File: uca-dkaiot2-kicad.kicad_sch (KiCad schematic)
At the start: 0 parts

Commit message: Continue filling schematics
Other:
- added sheet Input_Output (Input_Output.kicad_sch)
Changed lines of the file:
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@@
 	(title_block
 		(title "UCA DKAIoT2")
-		(date "2026-05-06")
+		(date "2026-05-27")
 		(rev "v0.1")
 		(company "//piernov")
@@
 				)
 			)
+		)
+	)
+	(sheet
+		(at 125.73 97.79)
+		(size 43.18 19.05)
+		(exclude_from_sim no)
+		(in_bom yes)
+		(on_board yes)
+		(dnp no)
+		(fields_autoplaced yes)
+		(stroke
+			(width 0.1524)
+			(type solid)
+		)
+		(fill
+			(color 0 0 0 0)
+		)
+		(property "Sheetname" "Input_Output"
+			(at 125.73 97.0784 0)
+			(show_name no)
+			(do_not_autoplace no)
+			(effects
+				(font
+					(size 1.27 1.27)
+				)
+				(justify left bottom)
+			)
+		)
+		(property "Sheetfile" "Input_Output.kicad_sch"
+			(at 125.73 117.4246 0)
+			(show_name no)
+			(do_not_autoplace no)
+			(effects
+				(font
+					(size 1.27 1.27)
+				)
+				(justify left top)
+			)
+		)
+		(instances
+			(project "uca-dkaiot2-kicad"
+				(path "/13b7de53-ecff-4b32-b513-b5b471d022a3"
+					(page "7")
+				)
+			)

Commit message: PCB component placement according to AIoT2
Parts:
- added H1, H2, H3, H4: MountingHole_Pad, MountingHole:MountingHole_3mm_Pad_Via, symbol Mechanical:MountingHole_Pad
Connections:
- new net GND: H1.1, H2.1, H3.1, H4.1

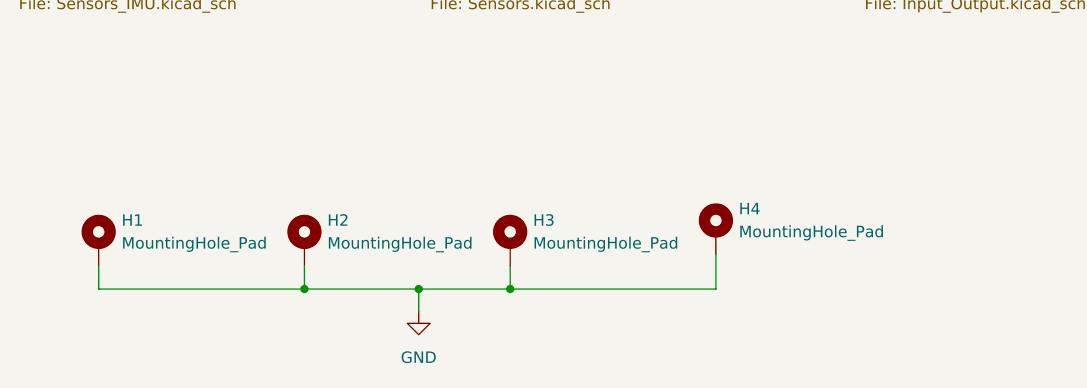
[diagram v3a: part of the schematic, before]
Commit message: pcb: start 2-layer routing
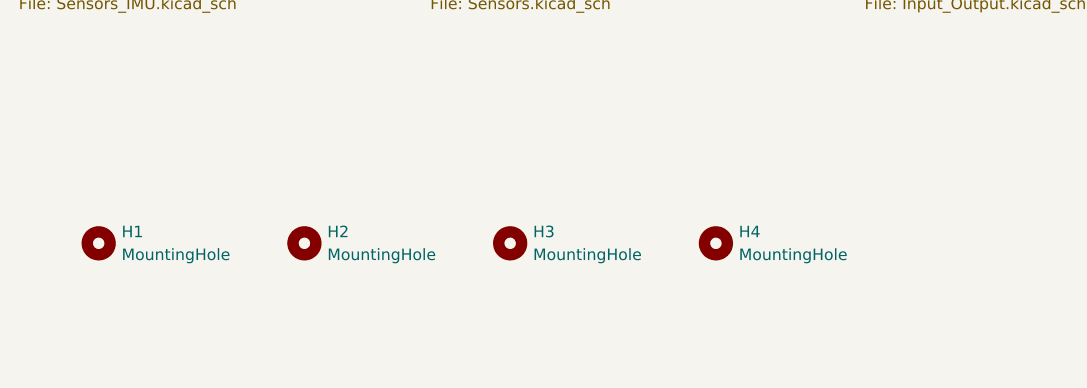
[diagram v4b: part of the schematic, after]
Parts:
- H1, H2, H3, H4: value MountingHole_Pad -> MountingHole; footprint MountingHole:MountingHole_3mm_Pad_Via -> MountingHole:MountingHole_3mm; symbol Mechanical:MountingHole_Pad -> Mechanical:MountingHole
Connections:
- removed net GND: H1.1, H2.1, H3.1, H4.1

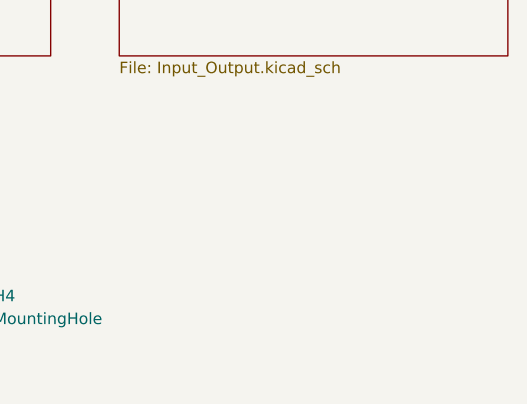
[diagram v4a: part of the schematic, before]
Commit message: Add OSHW logo
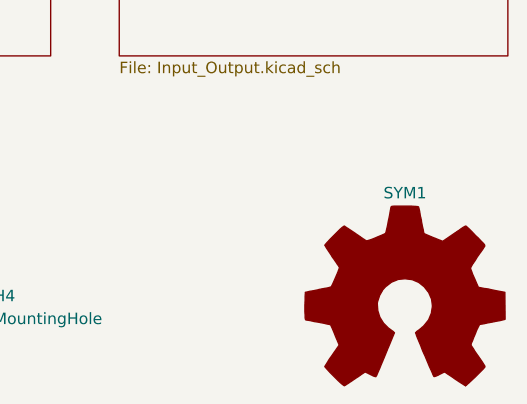
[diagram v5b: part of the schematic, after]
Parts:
- added SYM1: Logo_Open_Hardware_Large, footprints:OSHW-Logo_11.4x12mm_Copper_SolderMask, symbol Graphic:Logo_Open_Hardware_Large
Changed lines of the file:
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@@
+	)
+	(symbol
+		(lib_id "Graphic:Logo_Open_Hardware_Large")
+		(at 157.48 144.78 0)
+		(unit 1)
+		(body_style 1)
+		(exclude_from_sim no)
+		(in_bom no)
+		(on_board yes)
+		(in_pos_files yes)
+		(dnp no)
+		(fields_autoplaced yes)
+		(property "Reference" "SYM1"
+			(at 157.48 132.08 0)
+			(show_name no)
+			(do_not_autoplace no)
+			(effects
+				(font
+					(size 1.27 1.27)
+				)
+			)
+		)
+		(property "Value" "Logo_Open_Hardware_Large"
+			(at 157.48 154.94 0)
+			(hide yes)
+			(show_name no)
+			(do_not_autoplace no)
+			(effects
+				(font
+					(size 1.27 1.27)
+				)
+			)
+		)
+		(property "Footprint" "footprints:OSHW-Logo_11.4x12mm_Copper_SolderMask"
+			(at 157.48 144.78 0)
+			(hide yes)
+			(show_name no)
+			(do_not_autoplace no)
+			(effects
+				(font
+					(size 1.27 1.27)
+				)
+			)
+		)
+		(property "Datasheet" ""
+			(at 157.48 144.78 0)
+			(hide yes)
+			(show_name no)
+			(do_not_autoplace no)
+			(effects
+				(font
+					(size 1.27 1.27)
+				)
+			)
+		)
+		(property "Description" "Open Hardware logo, large"
+			(at 157.48 144.78 0)
+			(hide yes)
+			(show_name no)
+			(do_not_autoplace no)
+			(effects
+				(font
+					(size 1.27 1.27)
+				)
+			)
+		)
+		(property "Sim.Enable" "0"
+			(at 157.48 144.78 0)
+			(hide yes)
+			(show_name no)
+			(do_not_autoplace no)
+			(effects
+				(font
+					(size 1.27 1.27)
+				)
+			)
+		)
+		(instances
+			(project "uca-dkaiot2-kicad"
+				(path "/13b7de53-ecff-4b32-b513-b5b471d022a3"
+					(reference "SYM1")
+					(unit 1)
+				)
+			)
+		)
 	)
 	(symbol
